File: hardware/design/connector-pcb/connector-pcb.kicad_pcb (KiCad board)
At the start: 2 copper layers, 42 x 13 mm, 7 parts, among them J1 JWPF B04B, J2 JWPF B03B/B02B, J3 Conn_01x03_Pin, J5 Conn_01x02_Pin, J6 Conn_01x02_Pin, J8 JWPF B03B/B02B, J9 Conn_01x03_Pin

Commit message: Finalizing hardware design
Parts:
- moved J5 57.2 mm to (92.7, 64.0)
- moved J6 57.2 mm to (92.7, 64.0)
- moved J3 57.2 mm to (115.0, 64.0)
- moved J9 57.2 mm to (115.0, 64.0)
- moved J1 56.8 mm to (88.2, 70.3)
- moved J2 56.8 mm to (107.2, 70.2)
- moved J8 56.8 mm to (122.2, 70.2)
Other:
- board size 42 x 13 mm -> 42 x 14 mm

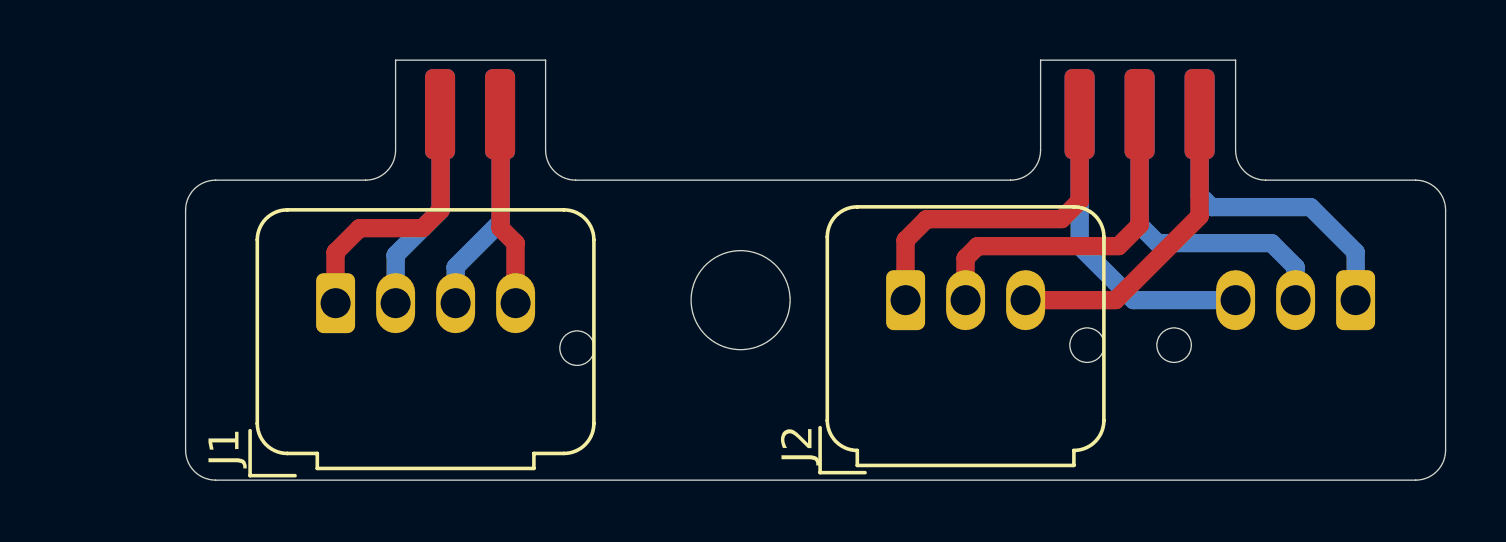
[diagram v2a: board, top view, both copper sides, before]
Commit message: Gen2.1 final hardware design (#16)
* New schematic done

Works with TLIN1028-Q1 transceiver
Added BMP581 pressure sensor
Removed 3wire output stage

* FInal ordered hardware

New 3pin connector
Extra 2pin connector for cadence measurement
No 3pin sensor variant
DC/DC converter for MCU
Pressure sensor
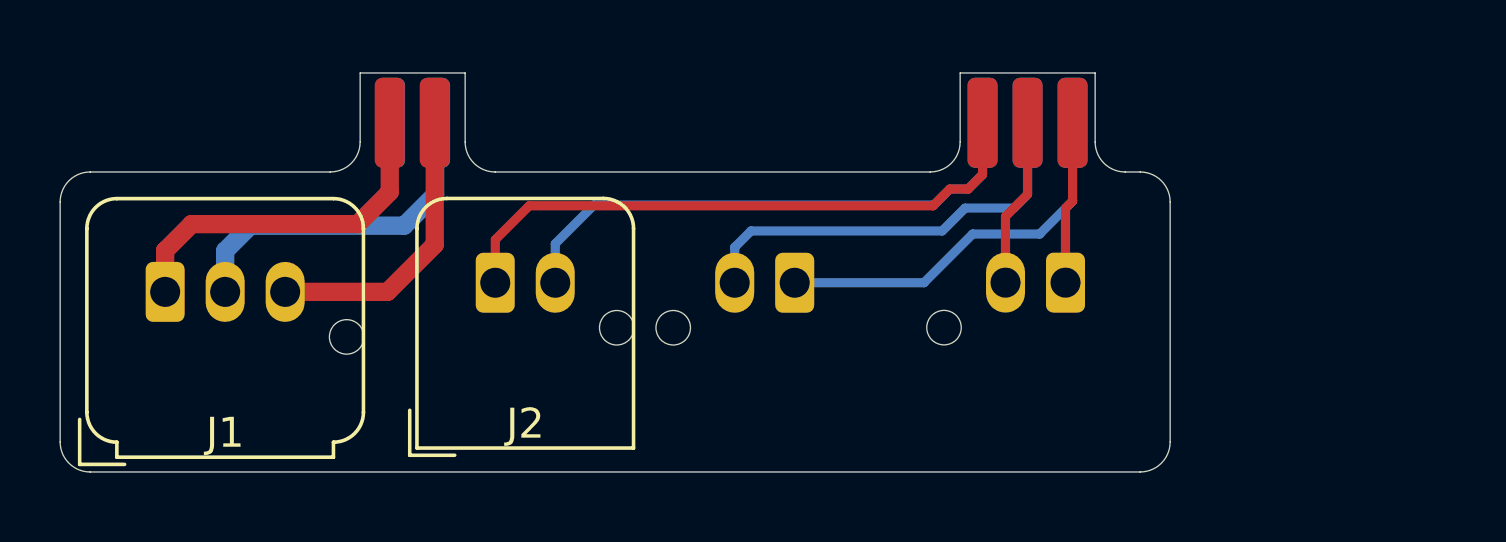
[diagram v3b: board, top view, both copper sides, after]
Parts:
- added J3: JWPF B02B, Connector_JST:JST_JWPF_B02B-JWPF-SK-R_1x02_P2.00mm_Vertical, B.Cu at (103.5, 69.6)
- J1: value JWPF B04B -> JWPF B03B; footprint Connector_JST:JST_JWPF_B04B-JWPF-SK-R_1x04_P2.00mm_Vertical -> Connector_JST:JST_JWPF_B03B-JWPF-SK-R_1x03_P2.00mm_Vertical
- J2: value JWPF B03B/B02B -> JWPF B02B; footprint Connector_JST:JST_JWPF_B03B-JWPF-SK-R_1x03_P2.00mm_Vertical -> Connector_JST:JST_JWPF_B02B-JWPF-SK-R_1x02_P2.00mm_Vertical
- J4: renamed from J8; value JWPF B03B/B02B -> JWPF B02B; footprint Connector_JST:JST_JWPF_B03B-JWPF-SK-R_1x03_P2.00mm_Vertical -> Connector_JST:JST_JWPF_B02B-JWPF-SK-R_1x02_P2.00mm_Vertical
- moved J2 13.7 mm to (93.5, 69.6)
- moved J4 9.69 mm to (112.5, 69.6)
- moved J1 5.69 mm to (82.5, 69.9)
- moved J9 3.74 mm to (111.3, 63.8)
- moved J10 3.74 mm to (111.3, 63.8)
- moved J14 1.94 mm to (90.8, 63.8)
- moved J5 1.93 mm to (90.8, 63.8), turned to 180 degrees
- renumbered J3 to J10, J6 to J14
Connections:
- J10 pad 2: Net-(J2-Pin_2) -> Net-(J10-Pin_2)
- J10 pad 3: Net-(J2-Pin_3) -> Net-(J10-Pin_3)
- J14 pad 2: Net-(J1-Pin_4) -> Net-(J1-Pin_3)
- J4 pad 1: Net-(J8-Pin_1) -> Net-(J10-Pin_3)
- J4 pad 2: Net-(J8-Pin_2) -> Net-(J10-Pin_2)
- J5 pad 2: Net-(J1-Pin_3) -> unconnected-(J5-Pin_2-Pad2)
- J9 pad 1: Net-(J8-Pin_1) -> Net-(J3-Pin_1)
- J9 pad 2: Net-(J8-Pin_2) -> Net-(J3-Pin_2)
- J9 pad 3: Net-(J8-Pin_3) -> Net-(J2-Pin_2)
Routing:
- net Net-(J3-Pin_2): track 0.00 -> 14.1 mm
- net Net-(J3-Pin_1): track 0.00 -> 13.0 mm
- net Net-(J10-Pin_1): track 10.3 -> 20.3 mm
- net Net-(J8-Pin_2): track 9.68 -> 0.00 mm
- net Net-(J2-Pin_3): track 9.46 -> 0.00 mm
- net Net-(J8-Pin_3): track 9.45 -> 0.00 mm
- net Net-(J8-Pin_1): track 9.39 -> 0.00 mm
- net Net-(J2-Pin_2): track 10.5 -> 18.2 mm
- net Net-(J10-Pin_2): track 0.00 -> 5.63 mm
- net Net-(J1-Pin_4): track 5.61 -> 0.00 mm
- net Net-(J1-Pin_2): track 6.02 -> 11.5 mm
- net Net-(J10-Pin_3): track 0.00 -> 5.43 mm
- net Net-(J1-Pin_1): track 8.08 -> 12.0 mm
- net Net-(J1-Pin_3): track 6.02 -> 9.70 mm
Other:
- board size 42 x 14 mm -> 37 x 13.3 mm
